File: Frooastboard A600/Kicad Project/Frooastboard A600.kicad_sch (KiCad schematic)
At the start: 204 parts, among them J1 PS2_5V, J3 SW Interface, J8 USB, Q1 BSS138, Q2 BSS138, U2 RP2040, U3 W25Q32JVZP, U4 LM317L_SOT-89, Y1 12MHz

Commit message: more led stuff NOT REVERSED YET
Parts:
- added D53: ST_LED1, LED_SMD:LED_PLCC-2_3.4x3.0mm_KA, symbol Device:LED
- added FPC3: AFA01-S04FCC-00, AFA01-SXXFCX-00:FPC-SMD_4P-P1.00_AFA01-S04FCC-00, symbol AFA01-SXXFCX-00:AFA01-S04FCC-00
- added R16: 1k, Resistor_SMD:R_0805_2012Metric, symbol Device:R_Small
- MX1: footprint MX_Hotswap:MX-Hotswap-1.5U -> MX_Solderable:MX-Solderable-1.5U
- MX10, MX15, MX19, MX21, MX26, MX32, MX37, MX4, MX41, MX42, MX48, MX55, MX6, MX60, MX67, MX8: footprint MX_Hotswap:MX-Hotswap-1.25U -> MX_Solderable:MX-Solderable-1.25U
- MX11, MX12, MX13, MX14, MX16, MX17, MX18, MX2, MX22, MX23, MX24, MX25, MX27, MX28, MX29, MX3, MX33, MX34, MX35, MX36, MX38, MX39, MX40, MX43, MX44, MX45, MX46, MX47, MX49, MX50, MX51, MX52, MX53, MX54, MX56, MX57, MX59, MX61, MX62, MX63, MX65, MX66, MX69, MX71, MX72, MX73, MX74, MX75, MX76, MX78, MX81, MX87, MX88, MX89, MX90, MX94: footprint MX_Hotswap:MX-Hotswap-1U -> MX_Solderable:MX-Solderable-1U
- MX30: footprint MX_Hotswap:MX-Hotswap-8U -> MX_Solderable:MX-Solderable-8U
- MX5: footprint MX_Hotswap:MX-Hotswap-2U -> MX_Solderable:MX-Solderable-2U
- MX58, MX7: footprint MX_Hotswap:MX-Hotswap-1.75U -> MX_Solderable:MX-Solderable-1.75U
- MX68: footprint MX_Hotswap:MX-Hotswap-ISO -> MX_Solderable:MX-Solderable-ISO
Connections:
- net GND: now also FPC3.4, FPC3.5, FPC3.6, R16.1
- net row0: now also U2.30 (GPIO19); no longer U2.29 (GPIO18)
- net at D26.2 (A), U2.35 (GPIO23): now also FPC3.1
- net at D16.2 (A), U2.36 (GPIO24): now also FPC3.2
- net at D6.2 (A), U2.37 (GPIO25): now also FPC3.3
- new net: D53.1 (K), R16.2
- new net CapsLock: D53.2 (A), U2.29 (GPIO18)
- no-connect marks 8 -> 7

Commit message: new leds (finally)
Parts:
- D16, D26, D6: footprint LED_SMD:LED_PLCC-2_3.4x3.0mm_KA -> Frooastboard Footprints:LED_RGB_SMD_6028_Reverse
- D53: value ST_LED1 -> CapsLock; footprint LED_SMD:LED_PLCC-2_3.4x3.0mm_KA -> Frooastboard Footprints:LED_RGB_SMD_6028_Reverse
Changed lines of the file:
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@@
 			)
 		)
-		(property "Value" "ST_LED1"
+		(property "Value" "CapsLock"
 			(at 159.258 114.046 90)
 			(effects
@@
 			)
 		)
-		(property "Footprint" "LED_SMD:LED_PLCC-2_3.4x3.0mm_KA"
+		(property "Footprint" "Frooastboard Footprints:LED_RGB_SMD_6028_Reverse"
 			(at 152.4 113.03 0)
 			(effects
@@
 			)
 		)
-		(property "Footprint" "LED_SMD:LED_PLCC-2_3.4x3.0mm_KA"
+		(property "Footprint" "Frooastboard Footprints:LED_RGB_SMD_6028_Reverse"
 			(at 139.7 113.03 0)
 			(effects
@@
 			)
 		)
-		(property "Footprint" "LED_SMD:LED_PLCC-2_3.4x3.0mm_KA"
+		(property "Footprint" "Frooastboard Footprints:LED_RGB_SMD_6028_Reverse"
 			(at 114.3 113.03 0)
 			(effects
@@
 			)
 		)
-		(property "Footprint" "LED_SMD:LED_PLCC-2_3.4x3.0mm_KA"
+		(property "Footprint" "Frooastboard Footprints:LED_RGB_SMD_6028_Reverse"
 			(at 127 113.03 0)
 			(effects

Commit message: bug fixes
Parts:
- MX30: footprint MX_Solderable:MX-Solderable-8U -> MX_Solderable:MX-Solderable-7U
- MX52: footprint MX_Solderable:MX-Solderable-1U -> MX_Solderable:MX-Solderable-1.25U
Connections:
- net RP_D+: now also USB1.6 (DP1), USB1.8 (DP2); no longer USB1.5 (DN2), USB1.7 (DN1)
- net RP_D-: now also USB1.5 (DN2), USB1.7 (DN1); no longer USB1.6 (DP1), USB1.8 (DP2)
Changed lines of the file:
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@@
 	(global_label "RP_D+"
 		(shape bidirectional)
-		(at 238.76 246.38 0)
+		(at 238.76 248.92 0)
 		(fields_autoplaced yes)
 		(effects
@@
 		)
 		(property "Intersheetrefs" "${INTERSHEET_REFS}"
-			(at 249.2065 246.38 0)
+			(at 249.2065 248.92 0)
 			(effects
 				(font
@@
 	(global_label "RP_D-"
 		(shape bidirectional)
-		(at 238.76 248.92 0)
+		(at 238.76 246.38 0)
 		(fields_autoplaced yes)
 		(effects
@@
 		)
 		(property "Intersheetrefs" "${INTERSHEET_REFS}"
-			(at 249.2065 248.92 0)
+			(at 249.2065 246.38 0)
 			(effects
 				(font
@@
 			)
 		)
-		(property "Footprint" "MX_Solderable:MX-Solderable-1U"
+		(property "Footprint" "MX_Solderable:MX-Solderable-1.25U"
 			(at 320.04 132.08 90)
 			(effects
@@
 			)
 		)
-		(property "Footprint" "MX_Solderable:MX-Solderable-8U"
+		(property "Footprint" "MX_Solderable:MX-Solderable-7U"
 			(at 281.94 132.08 90)
 			(effects

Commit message: move ralt
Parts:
- FPC1, J8: now not fitted
- FPC2: now fitted
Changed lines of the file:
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@@
 		(in_bom yes)
 		(on_board yes)
-		(dnp no)
+		(dnp yes)
 		(fields_autoplaced yes)
 		(property "Reference" "FPC1"
@@
 		(in_bom yes)
 		(on_board yes)
-		(dnp yes)
+		(dnp no)
 		(fields_autoplaced yes)
 		(property "Reference" "FPC2"
@@
 		(in_bom yes)
 		(on_board yes)
-		(dnp no)
+		(dnp yes)
 		(fields_autoplaced yes)
 		(property "Reference" "J8"

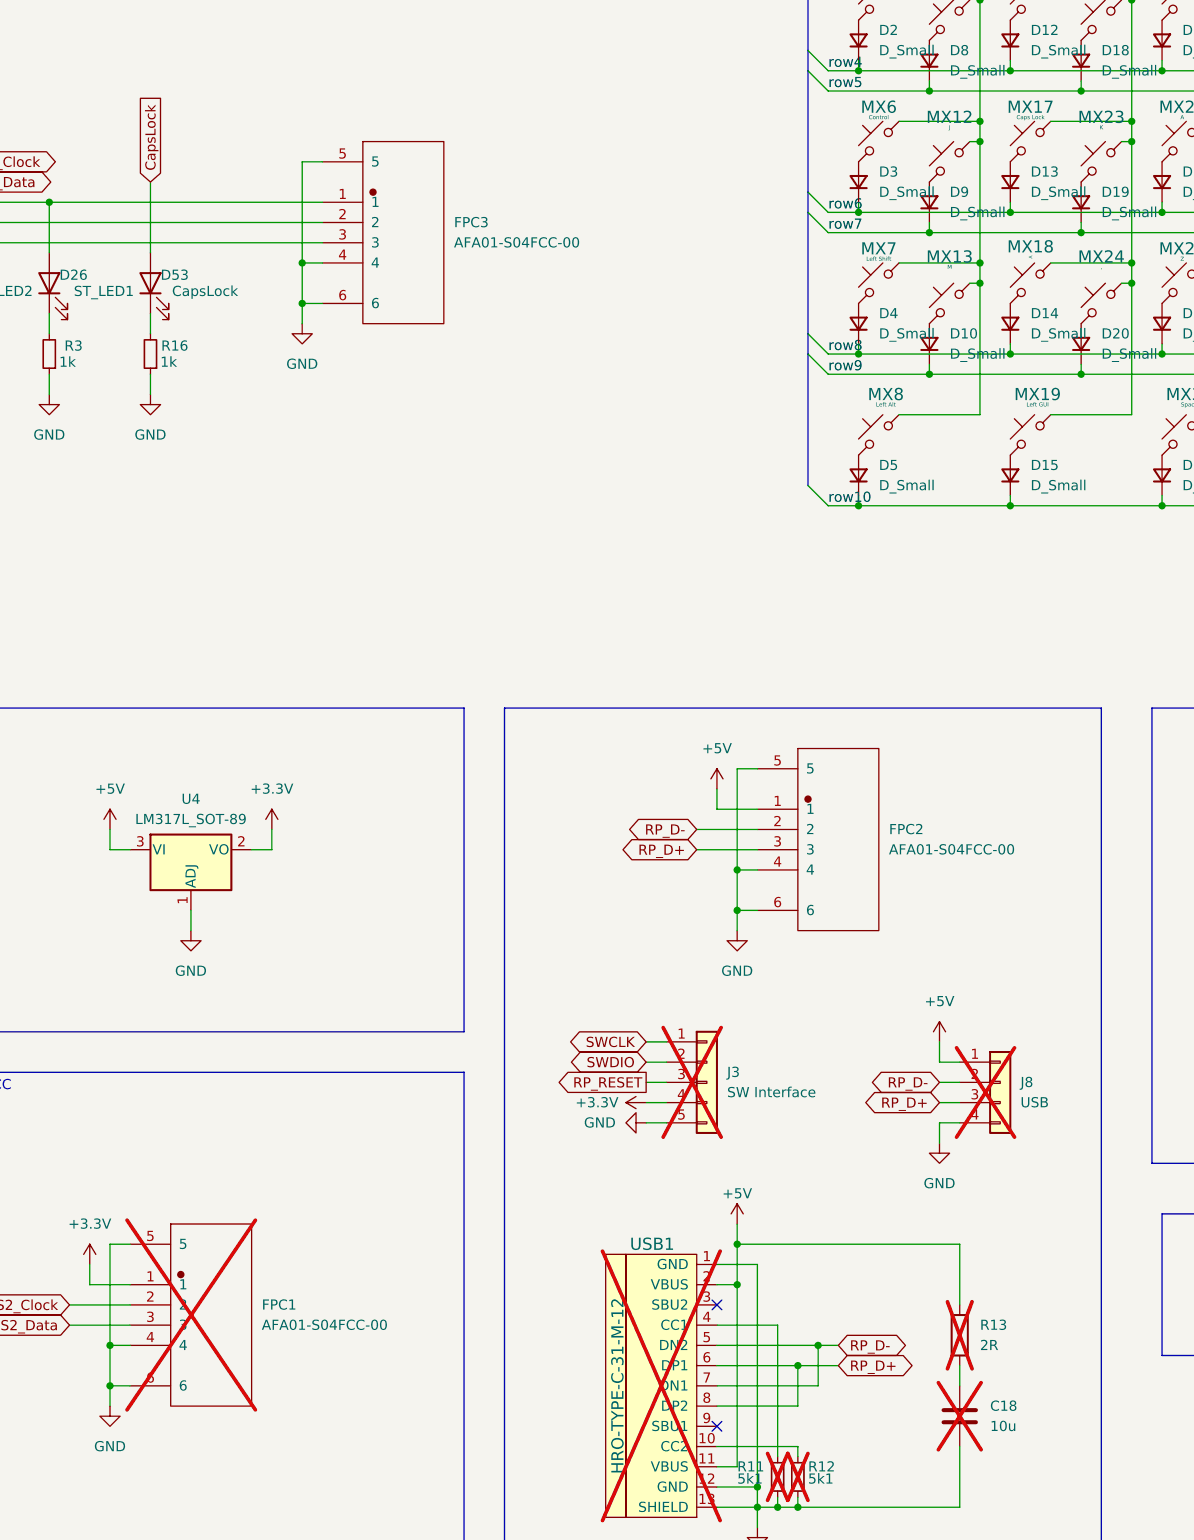
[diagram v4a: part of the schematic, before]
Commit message: fix 4pin (other still wrong)
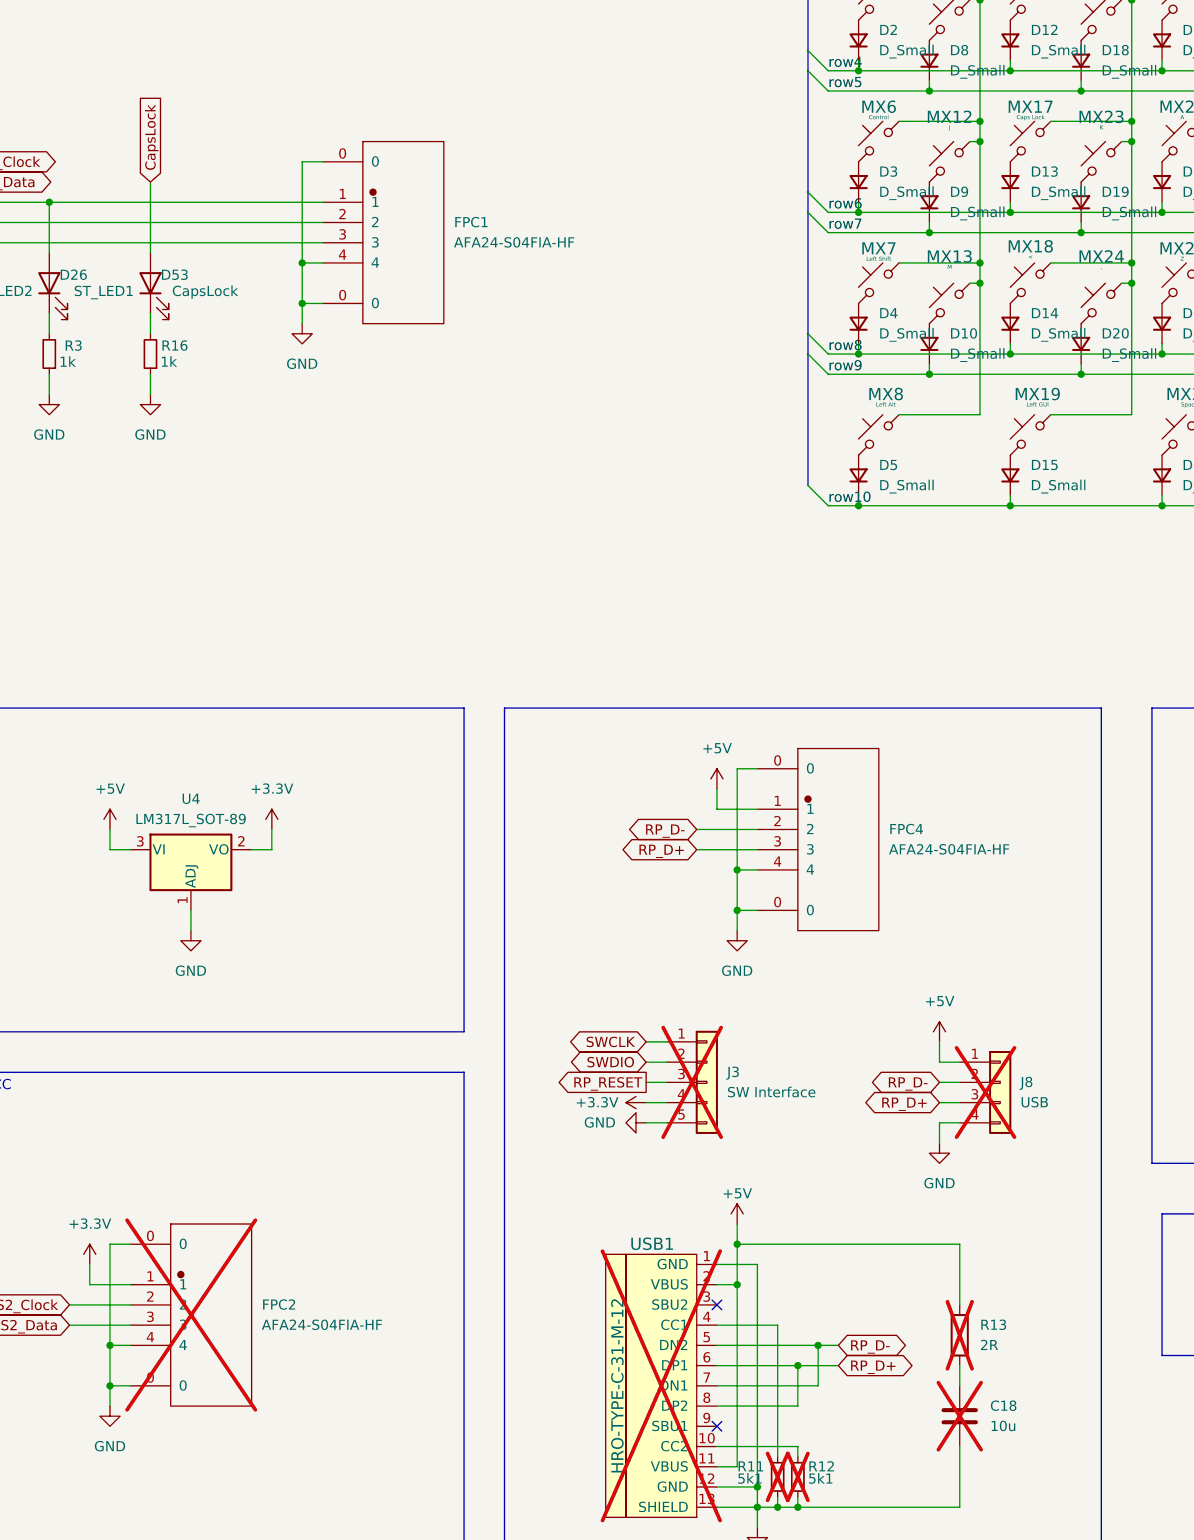
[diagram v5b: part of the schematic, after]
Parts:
- removed FPC1, FPC2, FPC3: AFA01-S04FCC-00, AFA01-SXXFCX-00:FPC-SMD_4P-P1.00_AFA01-S04FCC-00, symbol AFA01-SXXFCX-00:AFA01-S04FCC-00
- added FPC1, FPC2, FPC4: AFA24-S04FIA-HF, AFA24-SXXFIA-HF:FPC-SMD_4P-P1.00_AFA24-S04FIA-HF, symbol AFA24-SXXFIA-HF:AFA24-S04FIA-HF
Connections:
- net +3.3V: now also FPC2.1
- net +5V: now also FPC4.1
- net GND: now also FPC1.0, FPC1.4, FPC2.0, FPC2.4, FPC4.0, FPC4.4
- net PS2_Clock: now also FPC2.2
- net PS2_Data: now also FPC2.3
- net RP_D+: now also FPC4.3
- net RP_D-: now also FPC4.2
- net at D26.2 (A), U2.35 (GPIO23): now also FPC1.1
- net at D16.2 (A), U2.36 (GPIO24): now also FPC1.2
- net at D6.2 (A), U2.37 (GPIO25): now also FPC1.3

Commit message: prepare for pcba
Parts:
- C18, R11, R12, R13, USB1: now fitted
- R5, R6: now not fitted
- U4: LCSC Part # (none) -> C5120796
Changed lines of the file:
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@@
 		(in_bom yes)
 		(on_board yes)
-		(dnp yes)
+		(dnp no)
 		(property "Reference" "R12"
 			(at 234.95 261.62 0)
@@
 	)
 	(symbol
-		(lib_name "AFA24-SXXFIA-HF:AFA24-S04FIA-HF")
 		(lib_id "AFA24-SXXFIA-HF:AFA24-S04FIA-HF")
 		(at 236.22 182.88 0)
@@
 		(in_bom yes)
 		(on_board yes)
-		(dnp yes)
+		(dnp no)
 		(fields_autoplaced yes)
 		(property "Reference" "R13"
@@
 			)
 		)
+		(property "LCSC Part #" "C5120796"
+			(at 157.48 184.15 0)
+			(effects
+				(font
+					(size 1.27 1.27)
+				)
+				(hide yes)
+			)
+		)
 		(pin "1"
 		)
@@
 		(in_bom yes)
 		(on_board yes)
-		(dnp yes)
+		(dnp no)
 		(fields_autoplaced yes)
 		(property "Reference" "C18"
@@
 		(in_bom yes)
 		(on_board yes)
-		(dnp no)
+		(dnp yes)
 		(property "Reference" "R5"
 			(at 118.618 91.948 0)
@@
 		(in_bom yes)
 		(on_board yes)
-		(dnp yes)
+		(dnp no)
 		(property "Reference" "USB1"
 			(at 215.392 233.68 0)
@@
 	)
 	(symbol
-		(lib_name "AFA24-SXXFIA-HF:AFA24-S04FIA-HF")
 		(lib_id "AFA24-SXXFIA-HF:AFA24-S04FIA-HF")
 		(at 181.61 106.68 0)
@@
 		(in_bom yes)
 		(on_board yes)
-		(dnp yes)
+		(dnp no)
 		(property "Reference" "R11"
 			(at 226.06 261.62 0)
@@
 		(in_bom yes)
 		(on_board yes)
-		(dnp no)
+		(dnp yes)
 		(property "Reference" "R6"
 			(at 126.492 91.948 0)
@@
 	)
 	(symbol
-		(lib_name "AFA24-SXXFIA-HF:AFA24-S04FIA-HF")
 		(lib_id "AFA24-SXXFIA-HF:AFA24-S04FIA-HF")
 		(at 157.48 242.57 0)

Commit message: plate and afa01
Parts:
- removed D16: ST_LED2, Frooastboard Footprints:LED_RGB_SMD_6028_Reverse, symbol Device:LED
- removed D26: ST_LED1, Frooastboard Footprints:LED_RGB_SMD_6028_Reverse, symbol Device:LED
- removed D6: ST_LED3, Frooastboard Footprints:LED_RGB_SMD_6028_Reverse, symbol Device:LED
- removed R1, R15, R3: 1k, Resistor_SMD:R_0805_2012Metric, symbol Device:R_Small
- D1, D10, D100, D101, D102, D103, D104, D105, D106, D107, D11, D12, D13, D14, D15, D17, D18, D19, D2, D20, D21, D22, D23, D24, D25, D27, D28, D29, D3, D30, D31, D32, D33, D34, D35, D36, D37, D38, D39, D4, D40, D41, D42, D43, D44, D45, D46, D47, D48, D49, D5, D50, D51, D52, D54, D55, D56, D58, D59, D60, D61, D63, D67, D68, D69, D7, D70, D72, D8, D9, D92, D93, D94, D95, D96, D97, D98, D99: footprint Diode_SMD:D_0805_2012Metric -> Diode_SMD:D_SOD-323
- FPC1, FPC2, FPC4: footprint AFA24-SXXFIA-HF:FPC-SMD_4P-P1.00_AFA24-S04FIA-HF -> AFA01-SXXFCX-00:FPC-SMD_4P-P1.00_AFA01-S04FCC-00; symbol AFA24-SXXFIA-HF:AFA24-S04FIA-HF -> AFA01-SXXFCX-00:AFA01-S04FCC-00
- J1, J3, J8, Q1, Q2, R14, R2, R5, R6: now left out of the parts list
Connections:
- net GND: now also FPC1.5, FPC1.6, FPC2.5, FPC2.6, FPC4.5, FPC4.6; no longer FPC1.0, FPC2.0, FPC4.0

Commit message: iso rotated key
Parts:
- MX68: footprint MX_Solderable:MX-Solderable-ISO -> MX_Solderable:MX-Solderable-ISO-Rotated
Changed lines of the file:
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@@
 			)
 		)
-		(property "Footprint" "MX_Solderable:MX-Solderable-ISO"
+		(property "Footprint" "MX_Solderable:MX-Solderable-ISO-Rotated"
 			(at 347.98 80.01 90)
 			(effects
